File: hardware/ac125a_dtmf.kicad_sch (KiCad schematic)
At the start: 12 parts, among them J1 112-050-113R001

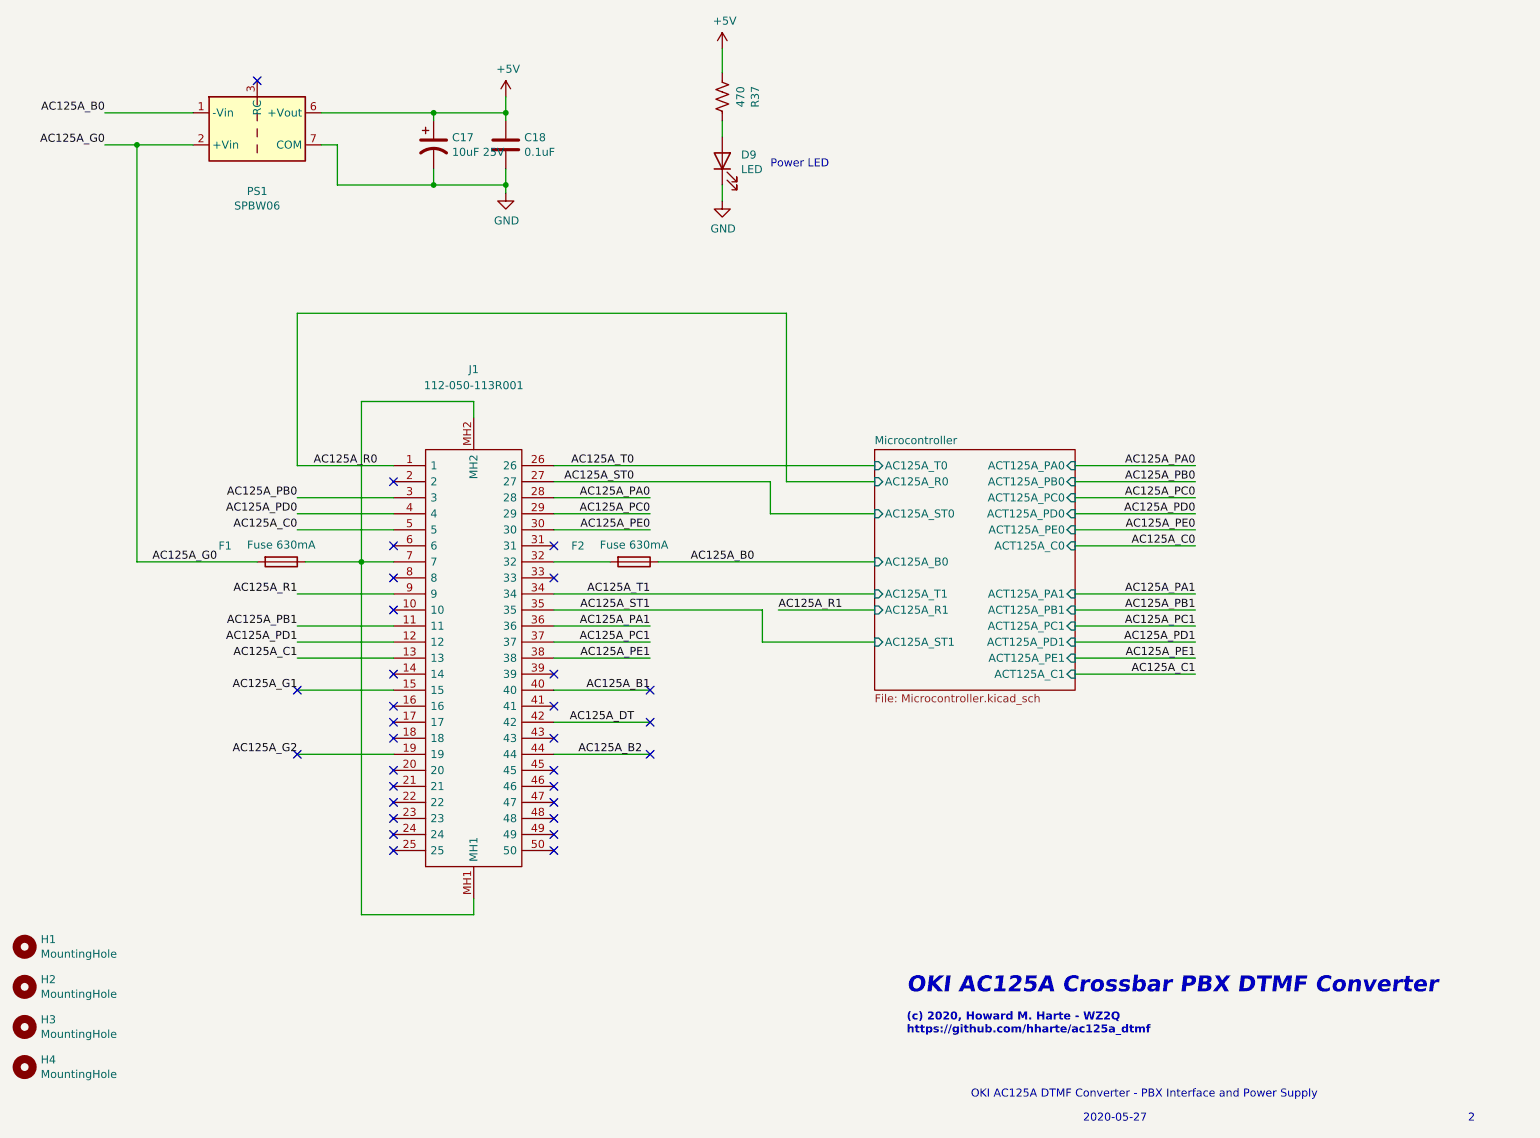
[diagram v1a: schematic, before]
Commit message: Issue 3: Utilize we755a_dtmf boards.
     * Carrier for 2*we755a_dtmf boards.
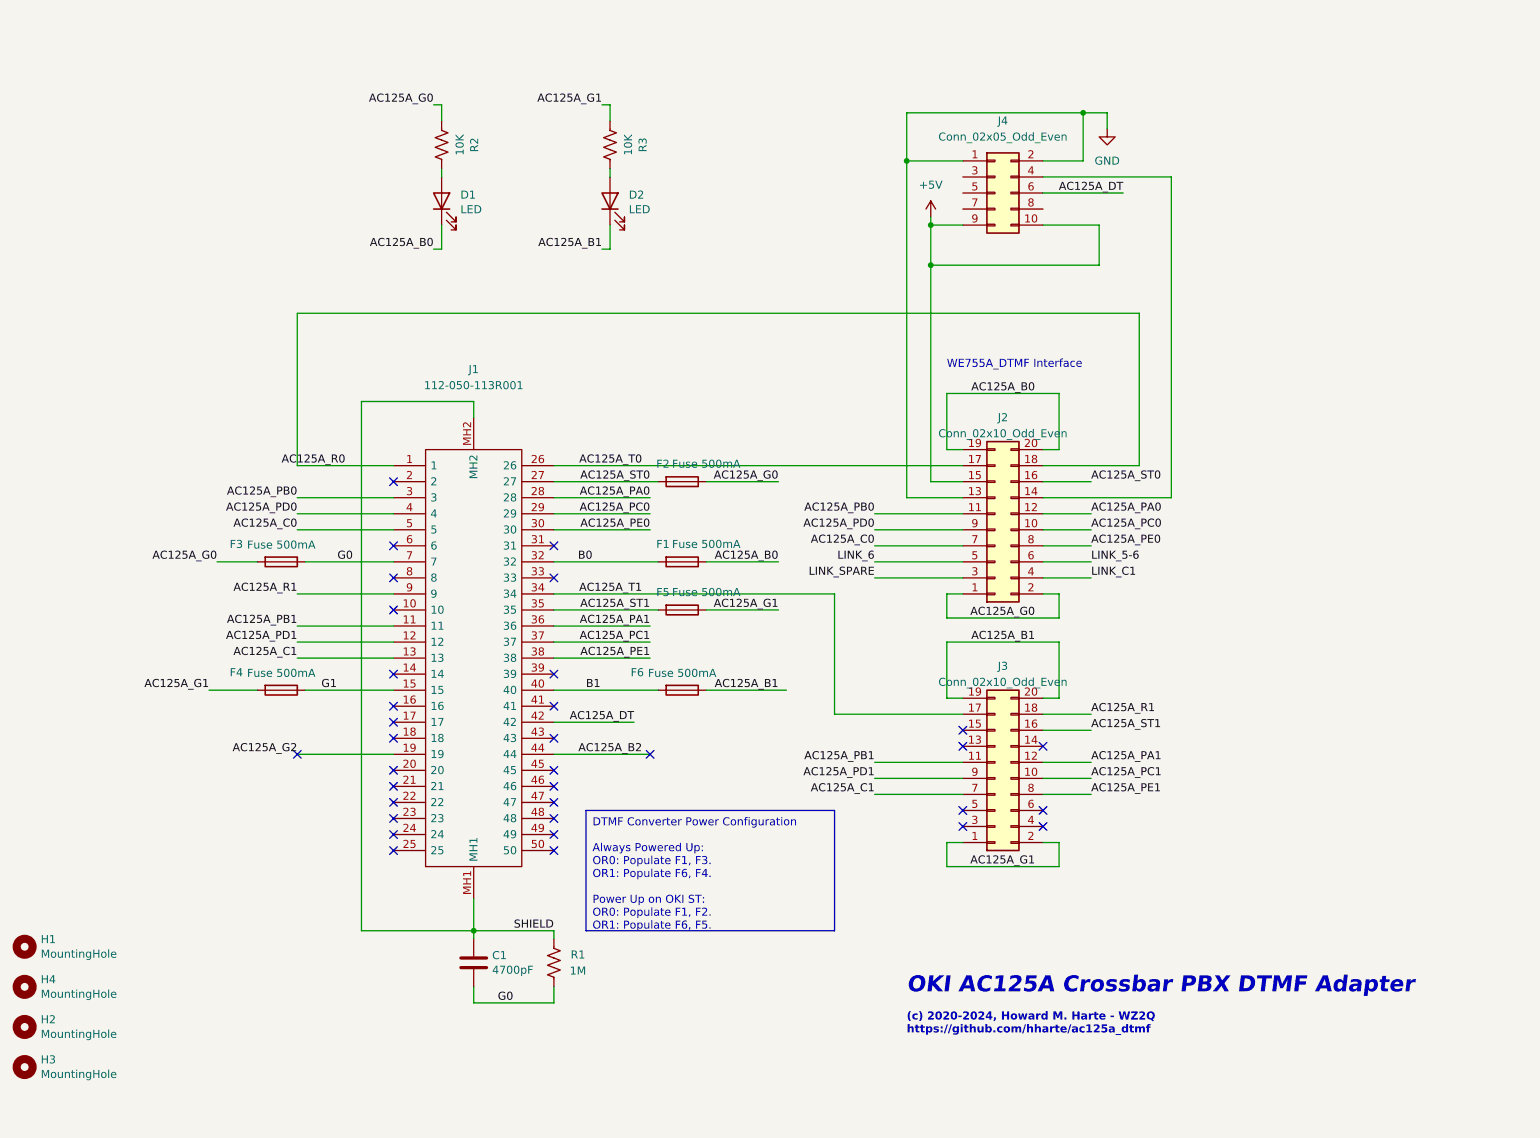
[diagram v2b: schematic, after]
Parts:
- removed C17: 10uF 25V, Capacitor_THT:CP_Radial_D6.3mm_P2.50mm, symbol ac125a_dtmf-rescue:CP1-Device
- removed C18: 0.1uF, Capacitor_THT:C_Disc_D3.0mm_W2.0mm_P2.50mm, symbol Device:C
- removed D9: LED, LED_THT:LED_D5.0mm, symbol Device:LED
- removed PS1: SPBW06, Converter_DCDC:Converter_DCDC_TRACO_TMR-xxxx_THT, symbol ac125a_dtmf:SPBW06
- removed R37: 470, Resistor_THT:R_Axial_DIN0207_L6.3mm_D2.5mm_P7.62mm_Horizontal, symbol Device:R_US
- added C1: 4700pF, Capacitor_THT:C_Disc_D4.3mm_W1.9mm_P5.00mm, symbol Device:C
- added D1, D2: LED, LED_THT:LED_D5.0mm, symbol Device:LED
- added F1, F4, F5, F6: Fuse 500mA, Resistor_THT:R_Axial_DIN0207_L6.3mm_D2.5mm_P10.16mm_Horizontal, symbol Device:Fuse
- added J2, J3: Conn_02x10_Odd_Even, ac125a_dtmf:WE755A-DTMF, symbol Connector_Generic:Conn_02x10_Odd_Even
- added J4: Conn_02x05_Odd_Even, Connector_PinHeader_2.54mm:PinHeader_2x05_P2.54mm_Vertical, symbol Connector_Generic:Conn_02x05_Odd_Even
- added R1: 1M, Resistor_THT:R_Axial_DIN0207_L6.3mm_D2.5mm_P7.62mm_Horizontal, symbol Device:R_US
- added R2, R3: 10K, Resistor_THT:R_Axial_DIN0207_L6.3mm_D2.5mm_P7.62mm_Horizontal, symbol Device:R_US
- F2: value Fuse 630mA -> Fuse 500mA; footprint Resistor_THT:R_Axial_DIN0309_L9.0mm_D3.2mm_P12.70mm_Horizontal -> Resistor_THT:R_Axial_DIN0207_L6.3mm_D2.5mm_P10.16mm_Horizontal; Digi-Key_PN (none) -> F2311-ND; MPN (none) -> 0251.500MXL
- F3: renamed from F1; value Fuse 630mA -> Fuse 500mA; footprint Resistor_THT:R_Axial_DIN0309_L9.0mm_D3.2mm_P12.70mm_Horizontal -> Resistor_THT:R_Axial_DIN0207_L6.3mm_D2.5mm_P10.16mm_Horizontal; Digi-Key_PN (none) -> F2311-ND; MPN (none) -> 0251.500MXL
- H1: footprint MountingHole:MountingHole_3.7mm_Pad -> MountingHole:MountingHole_2.7mm_Pad; now left out of the parts list
- H2: renamed from H3; footprint MountingHole:MountingHole_3.7mm_Pad -> MountingHole:MountingHole_2.7mm_Pad; now left out of the parts list
- H3: renamed from H4; footprint MountingHole:MountingHole_3.7mm_Pad -> MountingHole:MountingHole_2.7mm_Pad; now left out of the parts list
- H4: renamed from H2; footprint MountingHole:MountingHole_3.7mm_Pad -> MountingHole:MountingHole_2.7mm_Pad; now left out of the parts list
- J1: Digi-Key_PN (none) -> 1050RMA-ND; MPN (none) -> 112-050-113R001
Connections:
- net +5V: now also J2.15 (Pin_15), J4.10 (Pin_10), J4.9 (Pin_9)
- net AC125A_B0: now also D1.1 (K), F1.1, J2.19 (Pin_19), J2.20 (Pin_20); no longer F2.1
- net AC125A_B1: now also D2.1 (K), F6.1, J3.19 (Pin_19), J3.20 (Pin_20); no longer J1.40
- net AC125A_C0: now also J2.7 (Pin_7)
- net AC125A_C1: now also J3.7 (Pin_7)
- net AC125A_DT: now also J4.6 (Pin_6)
- net AC125A_G0: now also F2.1, J2.1 (Pin_1), J2.2 (Pin_2), R2.2
- net AC125A_G1: now also F4.2, F5.1, J3.1 (Pin_1), J3.2 (Pin_2), R3.2; no longer J1.15
- net AC125A_PA0: now also J2.12 (Pin_12)
- net AC125A_PA1: now also J3.12 (Pin_12)
- net AC125A_PB0: now also J2.11 (Pin_11)
- net AC125A_PB1: now also J3.11 (Pin_11)
- net AC125A_PC0: now also J2.10 (Pin_10)
- net AC125A_PC1: now also J3.10 (Pin_10)
- net AC125A_PD0: now also J2.9 (Pin_9)
- net AC125A_PD1: now also J3.9 (Pin_9)
- net AC125A_PE0: now also J2.8 (Pin_8)
- net AC125A_PE1: now also J3.8 (Pin_8)
- net AC125A_R0: now also J2.18 (Pin_18)
- net AC125A_R1: now also J3.18 (Pin_18)
- net AC125A_ST0: now also F2.2, J2.16 (Pin_16)
- net AC125A_ST1: now also F5.2, J3.16 (Pin_16)
- net AC125A_T0: now also J2.17 (Pin_17)
- net AC125A_T1: now also J3.17 (Pin_17)
- net GND: now also J2.13 (Pin_13), J4.1 (Pin_1), J4.2 (Pin_2)
- net B0: now reaches J1.32
- net B0: now also F1.2; no longer F2.2
- net G0: now reaches F3.1, J1.7
- net G0: now also C1.2, R1.2; no longer J1.MH1, J1.MH2
- new net: D2.2 (A), R3.1
- new net: D1.2 (A), R2.1
- new net: J2.14 (Pin_14), J4.4 (Pin_4)
- new net B1: F6.2, J1.40
- new net G1: F4.1, J1.15
- new net LINK_5-6: J2.6 (Pin_6)
- new net LINK_6: J2.5 (Pin_5)
- new net LINK_C1: J2.4 (Pin_4)
- new net LINK_SPARE: J2.3 (Pin_3)
- new net SHIELD: C1.1, J1.MH1, J1.MH2, R1.1
- no-connect marks 31 -> 34
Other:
- removed sheet Microcontroller
- note added: "(c) 2020-2024, Howard M. Harte - WZ2Q https://github.com/hharte/ac125a_dtmf"
- note added: "OKI AC125A Crossbar PBX DTMF Adapter"
- note added: "WE755A_DTMF Interface"
- note removed: "(c) 2020, Howard M. Harte - WZ2Q https://github.com/hharte/ac125a_dtmf"
- note removed: "2"
- note removed: "2020-05-27"
- note removed: "OKI AC125A Crossbar PBX DTMF Converter"
- note removed: "OKI AC125A DTMF Converter - PBX Interface and Power Supply"
- note removed: "Power LED"
- title: (none) -> OKI AC125A DTMF Adapter
